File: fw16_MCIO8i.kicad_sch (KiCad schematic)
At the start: 24 parts

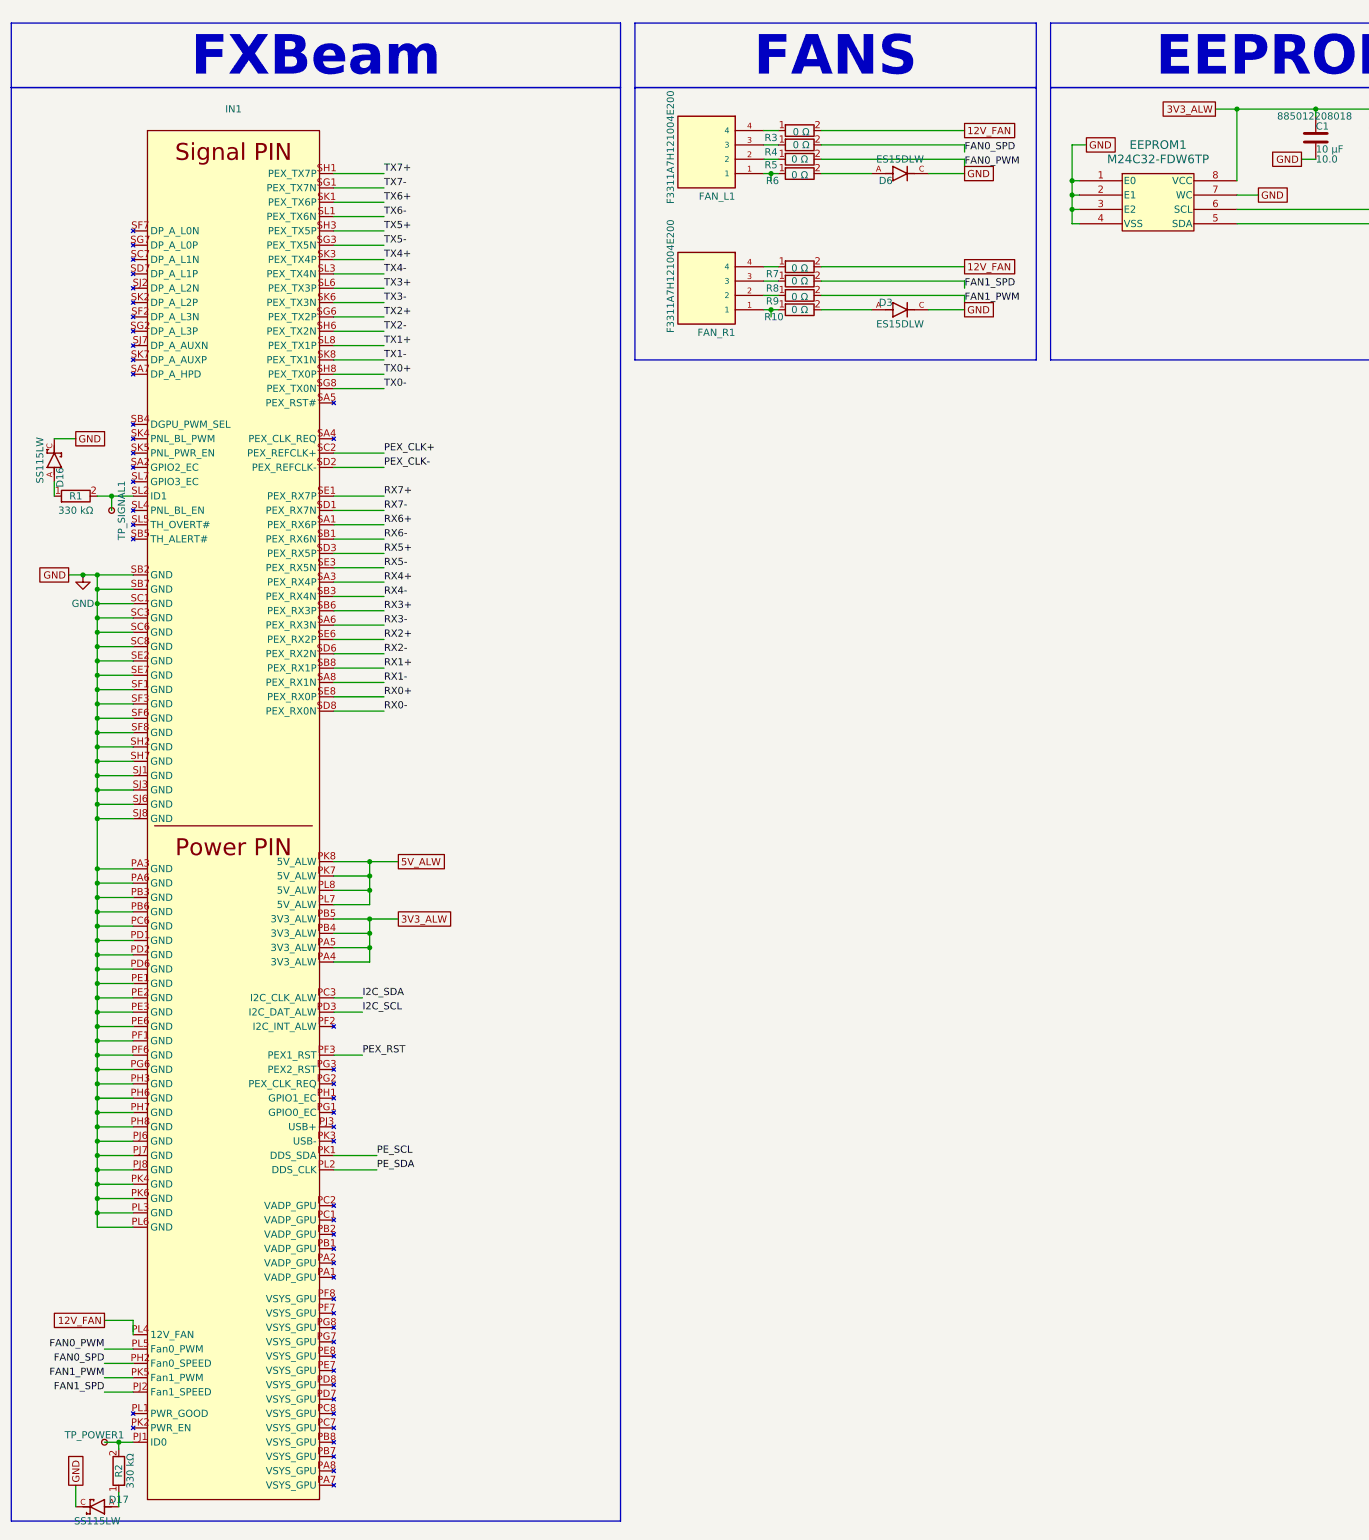
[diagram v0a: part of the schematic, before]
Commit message: Fixed EEPROM error
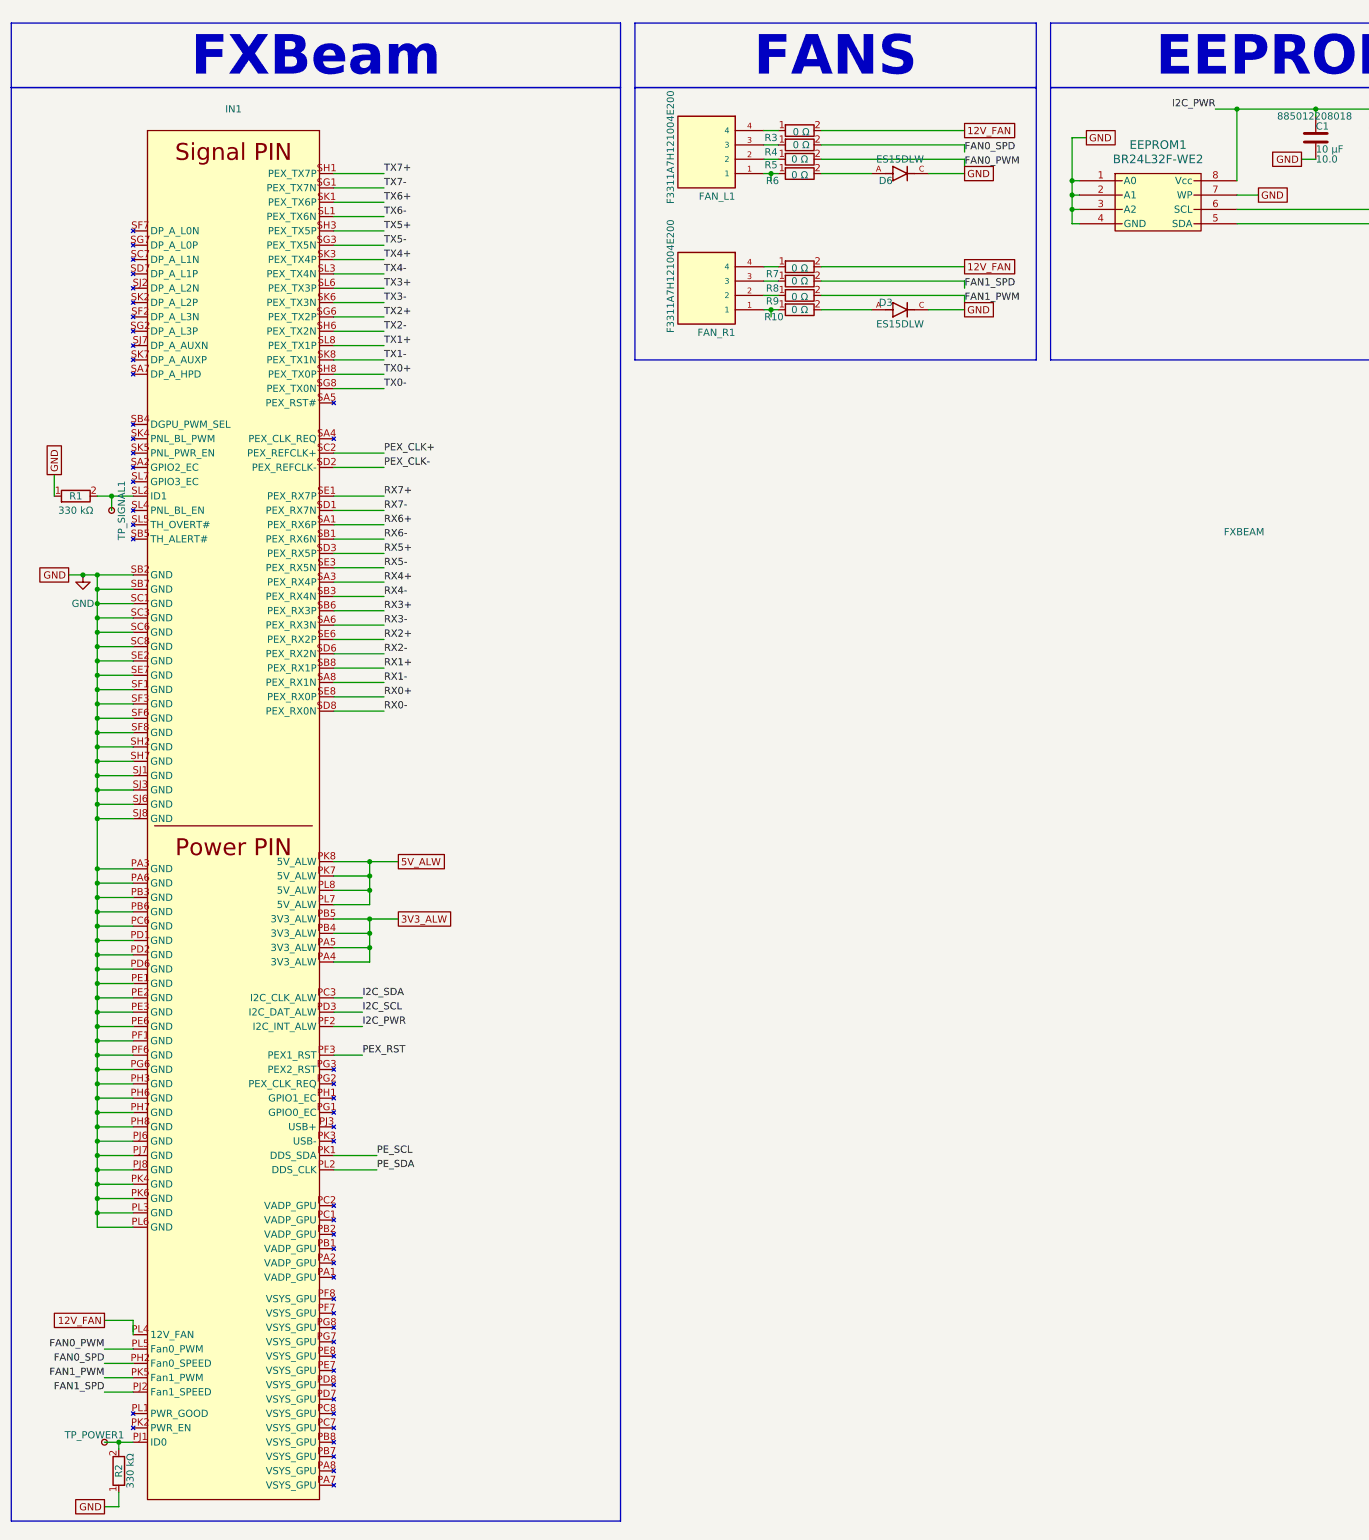
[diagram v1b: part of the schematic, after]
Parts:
- removed D16, D17: SS115LW, diode:DIO_SS115LW, symbol diode:SS115LW
- removed EEPROM1: M24C32-FDW6TP, eeprom:TSSOP8_4P5X3P1X0P65_STM, symbol eeprom:M24C32-FDW6TP
- added EEPROM1: BR24L32F-WE2, eeprom:SOP8_ROM, symbol eeprom:BR24L32F-WE2
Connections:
- net 3V3_ALW: no longer C1.1, R11.2, R12.2
- net GND: now also R1.1, R2.1, EEPROM1.1 (A0), EEPROM1.2 (A1), EEPROM1.3 (A2), EEPROM1.4 (GND), EEPROM1.7 (WP)
- net I2C_SCL: now also EEPROM1.6 (SCL)
- net I2C_SDA: now also EEPROM1.5 (SDA)
- net I2C_PWR: now reaches IN1.PF2 (I2C_INT_ALW)
- net I2C_PWR: now also C1.1, R11.2, R12.2, EEPROM1.8 (Vcc)

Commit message: Schematics fixed
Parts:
- removed C1: 1206_H1.6_885012208018, capacitor:C_Wurth_WCAP-CSGP-1206_H1.6, symbol capacitor:1206_H1.6_885012208018
- removed R11, R12: 1206_R_560112132018, resistors:R_Wurth_WRIS-RSKS-1206_R, symbol resistor:1206_R_560112132018
- FXBEAM1: renamed from IN1; value FXBEAM -> (none); footprint expansion_bay:FXBeam -> (none)
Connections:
- net I2C_SCL: now also FXBEAM1.PC3 (I2C_CLK_ALW); no longer FXBEAM1.PD3 (I2C_DAT_ALW)
- net I2C_SDA: now also FXBEAM1.PD3 (I2C_DAT_ALW); no longer FXBEAM1.PC3 (I2C_CLK_ALW)

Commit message: New routing
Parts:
- IN1: renamed from FXBEAM1; value (none) -> FXBEAM; footprint (none) -> expansion_bay:FXBeam
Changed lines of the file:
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@@
 		(on_board yes)
 		(dnp no)
-		(property "Reference" "FXBEAM1"
+		(property "Reference" "IN1"
 			(at 55.88 31.75 0)
 			(effects
@@
 			)
 		)
-		(property "Value" ""
-			(at 234.95 106.68 0)
-			(effects
-				(font
-					(size 1.27 1.27)
-				)
-			)
-		)
-		(property "Footprint" ""
+		(property "Value" "FXBEAM"
+			(at 55.88 34.036 0)
+			(effects
+				(font
+					(size 1.27 1.27)
+				)
+			)
+		)
+		(property "Footprint" "expansion_bay:FXBeam"
 			(at 234.95 106.68 0)
 			(effects
@@
 			(project "fw16_MCIO8i"
 				(path "/50f5fd03-67f8-43d1-8bfe-dca2cf908bf0"
-					(reference "FXBEAM1")
+					(reference "IN1")
 					(unit 1)
 				)

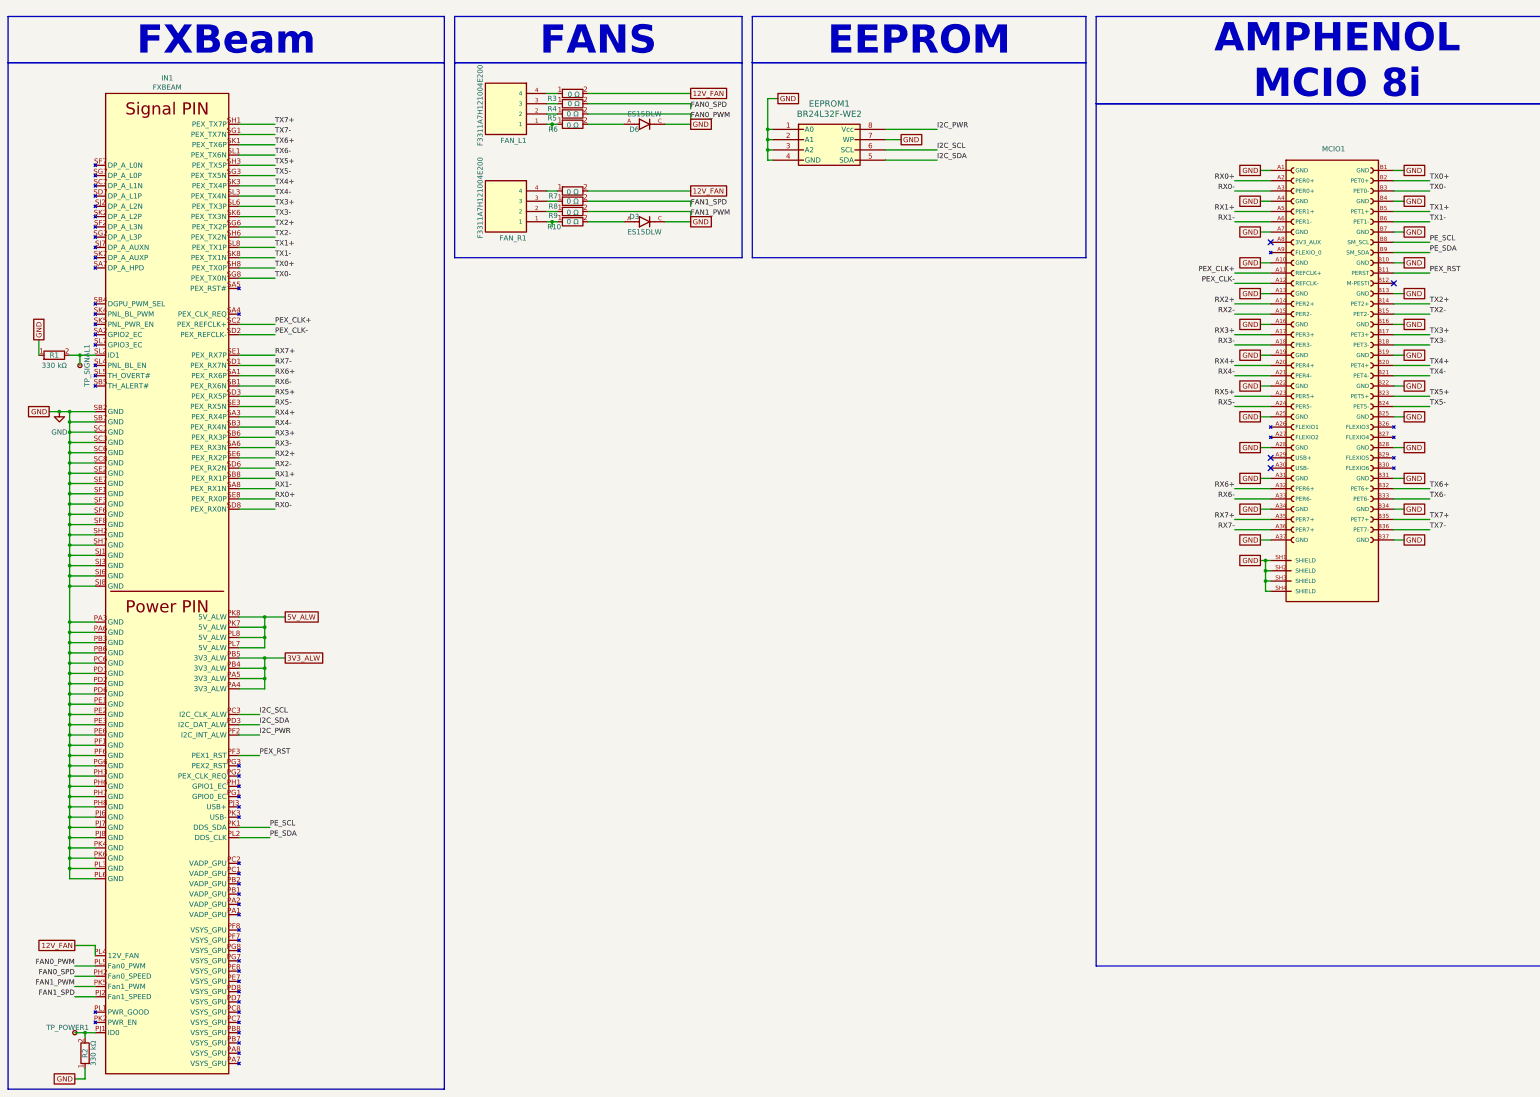
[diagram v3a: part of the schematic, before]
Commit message: Schematics revamped
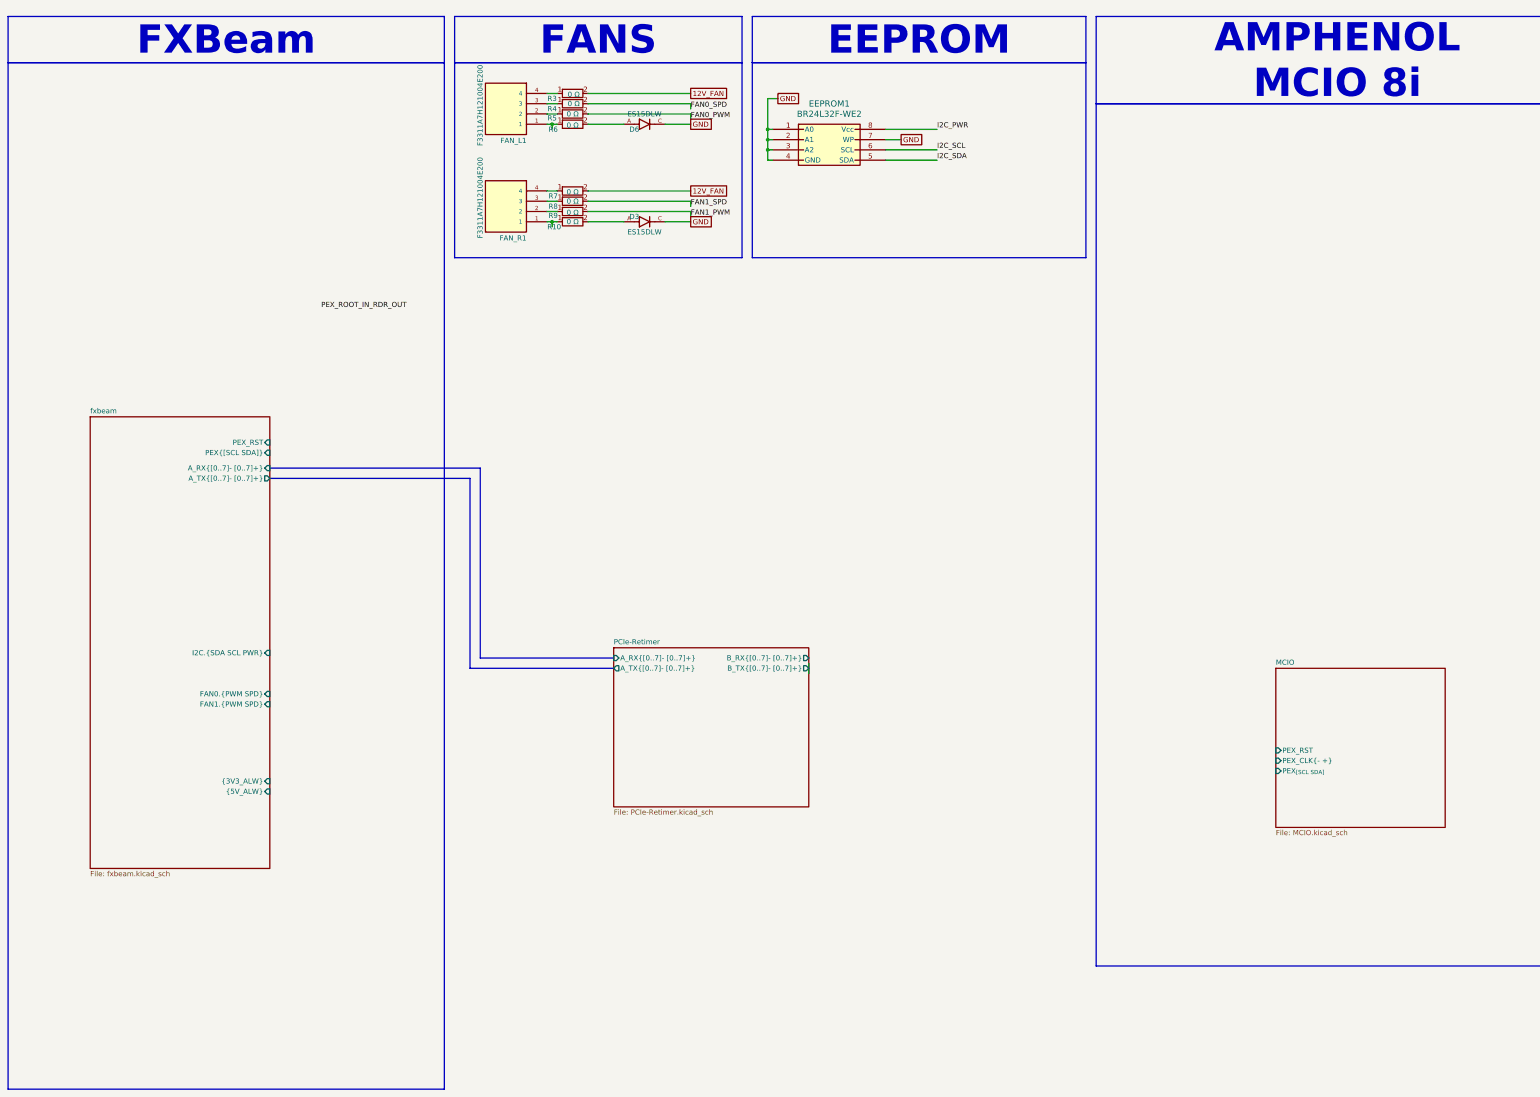
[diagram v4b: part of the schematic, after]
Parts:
- removed IN1: FXBEAM, expansion_bay:FXBeam, symbol expansion_bay:FXBeam
- removed MCIO1: G97R22312HR, mcio-connector:AMPHENOL_G97R22312HR, symbol mcio-connector:G97R22312HR
- removed R1, R2: 1206_R_560112132036, resistors:R_Wurth_WRIS-RSKS-1206_R, symbol resistor:1206_R_560112132036
- removed TP_POWER1, TP_SIGNAL1: TestPoint_Small, TestPoint:TestPoint_Pad_D3.0mm, symbol Connector:TestPoint_Small
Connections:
- no-connect marks 4 -> 0
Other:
- added sheet MCIO (MCIO.kicad_sch)
- added sheet PCIe-Retimer (PCIe-Retimer.kicad_sch)
- added sheet fxbeam (fxbeam.kicad_sch)
